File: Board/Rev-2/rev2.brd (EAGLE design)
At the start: 148.6 x 63.2 mm, 56 parts, among them IC1 74HC595N, T1 2N3904, T2 2N3904, T3 2N3904, T4 2N3904, T5 2N3904, T6 2N3904, T7 2N3904, T8 2N3904

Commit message: Board Generated
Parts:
- removed ESP-RESET, RESET: tackswitch, buttons:B3F-10XX
- removed PHOTOREG: 1kohm, resistor:0204/7
- removed R1: PHOTOCELLONB, LDR:ON_BOARD
- removed SL1: Flash, con-amp-quick:02PA
- added FLASH, GND_SWITCH, VCC_SWITCH: TOGGLE_SWITCH, Toggle Switch:TOGGLE_SWITCH
- added MCU-RESET, SETUP_MODE: tackswitch, buttons:B3F-10XX
- added PHOTO_REG: PHOTOCELLONB, LDR:ON_BOARD
- added PULLUP: 10kohm, resistor:0204/7
- added RESET_REG: 1kohm, resistor:0204/7
- added SV1: (no value), con-lstb:MA04-1
- moved RELR8 31.2 mm to (51.1, 24.0), turned to 90 degrees
- moved RELR6 29.3 mm to (94.8, 26.0), turned to 90 degrees
- moved D3 28.6 mm to (97.0, 15.1)
- moved RELR7 28.5 mm to (70.9, 27.0), turned to 90 degrees
- moved RELR5 28.3 mm to (117.7, 27.0), turned to 90 degrees
- moved D4 27.6 mm to (73.2, 16.1)
- moved D2 27.5 mm to (118.9, 15.1)
- moved D1 25.9 mm to (143.0, 14.1)
- moved PULLDOWN 24.9 mm to (20.0, 50.8)
- moved C1 24.9 mm to (13.6, 49.5)
- moved T5 24.7 mm to (119.3, 60.1)
- moved T6 24.7 mm to (96.4, 60.1)
- moved T8 24.7 mm to (50.7, 60.1)
- moved U$2 24.7 mm to (144.7, 29.2)
- moved CON-REL-1 24.7 mm to (135.8, 3.77)
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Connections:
- new net N$55: GND_SWITCH.ON, SV1.1
- new net N$56: SV1.4, VCC_SWITCH.ON
- net 3.5V: now also FLASH.OFF, PHOTO_REG.1, PULLUP.2, SETUP_MODE.2; no longer R1.1, RESET.2
- net ADC: now also PHOTO_REG.2, RESET_REG.2; no longer PHOTOREG.2, R1.2
- net GND: now also FLASH.ON, GND_SWITCH.IN, MCU-RESET.4, PULLUP.1, RESET_REG.1; no longer ESP-RESET.4, PHOTOREG.1, SL1.1
- net N$26: now also SETUP_MODE.4; no longer RESET.4
- net N$28: now also FLASH.IN; no longer SL1.2
- net N$29: now also SETUP_MODE.3; no longer RESET.3
- net N$31: now also MCU-RESET.2; no longer ESP-RESET.2
- net RX: now also SV1.2
- net TX: now also SV1.3
- net VCC: now also VCC_SWITCH.IN
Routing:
- net RX: track 52.8 -> 175.5 mm, vias 0 -> 7
- net TX: track 60.3 -> 167.4 mm, vias 0 -> 8
- net GND: track 399.1 -> 492.8 mm, vias 0 -> 1
- net N$47: track 30.0 -> 79.1 mm, vias 0 -> 3
- net N$27: track 34.1 -> 69.1 mm, vias 1 -> 0
- net N$55: track 0.00 -> 33.6 mm
- net N$28: track 44.2 -> 75.7 mm, vias 1 -> 0
- net N$48: track 32.0 -> 63.2 mm, vias 0 -> 1
- net RELAY7: track 78.2 -> 48.7 mm, vias 2 -> 1
- net VCC: track 206.3 -> 234.3 mm, vias 0 -> 1
- net N$49: track 33.5 -> 59.7 mm, vias 0 -> 1
- net RELAY1: track 121.2 -> 144.6 mm, vias 0 -> 3
- net N$56: track 0.00 -> 22.3 mm
- net 3.5V: track 266.5 -> 285.4 mm, vias 2 -> 6
- net SHCP: track 44.3 -> 61.8 mm, vias 3 -> 1
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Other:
- board size 148.6 x 63.2 mm -> 150.6 x 63.2 mm
- board text added: "Live"
- board text added: "Nutral"

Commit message: board updated
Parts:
- SV1: device con-lstb:MA04-1 -> con-lstb:MA06-2
- moved D1 7.28 mm to (141.0, 7.12)
- moved IC1 6.00 mm to (31.5, 6.31)
- moved U$1 5.00 mm to (14.6, 1.31), turned to 180 degrees
- moved PULLUP 4.00 mm to (22.0, 56.8), turned to 0 degrees
- moved T4 4.00 mm to (47.7, 5.85)
- moved REG1 2.83 mm to (22.0, 53.6)
- moved GND_SWITCH 2.24 mm to (141.0, 41.8)
- moved PULLDOWN 2.24 mm to (22.0, 49.8)
- moved U$2 2.24 mm to (143.7, 31.2)
- moved VCC_SWITCH 2.24 mm to (146.0, 41.8)
- moved SV1 1.54 mm to (146.0, 15.0), turned to 270 degrees
- moved D5 1.00 mm to (142.0, 55.3)
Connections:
- net 3.5V: now also SV1.4
- net CS0: now also SV1.6
- net GPIO10: now also SV1.7
- net GPIO5: now also SV1.5
- net GPIO9: now also SV1.9
- net MISO: now also SV1.8
- net MOSI: now also SV1.10
- net N$55: now also SV1.12; no longer SV1.1
- net N$56: now also SV1.2; no longer SV1.4
- net RX: now also SV1.3; no longer SV1.2
- net SCLK: now also SV1.11
- net TX: now also SV1.1; no longer SV1.3
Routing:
- net MISO: track 0.00 -> 211.1 mm, vias 0 -> 4
- net GPIO5: track 0.00 -> 175.1 mm, vias 0 -> 7
- net MOSI: track 0.00 -> 156.5 mm, vias 0 -> 7
- net GPIO9: track 0.00 -> 147.1 mm, vias 0 -> 7
- net GPIO10: track 0.00 -> 135.6 mm, vias 0 -> 6
- net CS0: track 0.00 -> 133.1 mm, vias 0 -> 11
- net SCLK: track 0.00 -> 123.4 mm, vias 0 -> 6
- net N$28: track 75.7 -> 42.5 mm, vias 0 -> 1
- net N$47: track 79.1 -> 48.8 mm, vias 3 -> 0
- net VCC: track 234.3 -> 262.4 mm
- net N$49: track 59.7 -> 34.3 mm
- net GND: track 492.8 -> 517.2 mm, vias 1 -> 2
- net RX: track 175.5 -> 199.2 mm, vias 7 -> 6
- net STCP: track 39.0 -> 59.0 mm, vias 1 -> 2
- net N$48: track 63.2 -> 43.9 mm, vias 1 -> 0
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
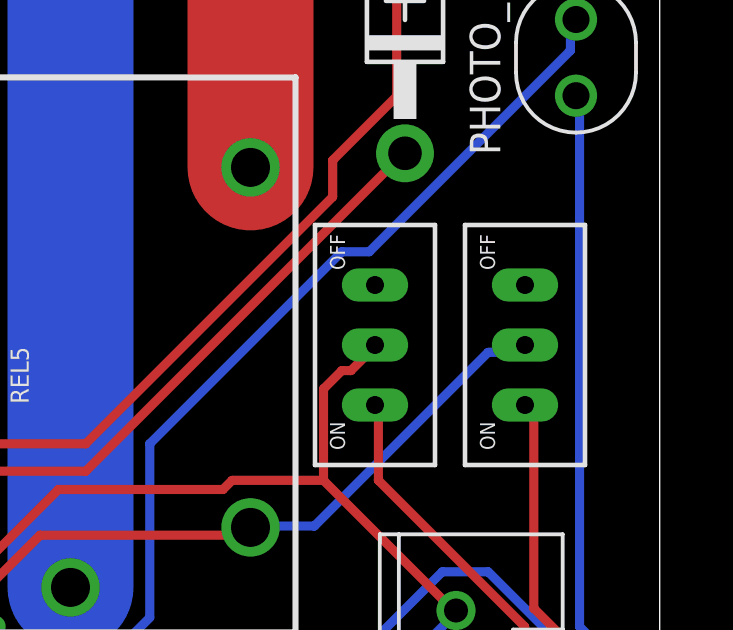
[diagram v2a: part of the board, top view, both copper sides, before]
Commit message: Reconnect option added
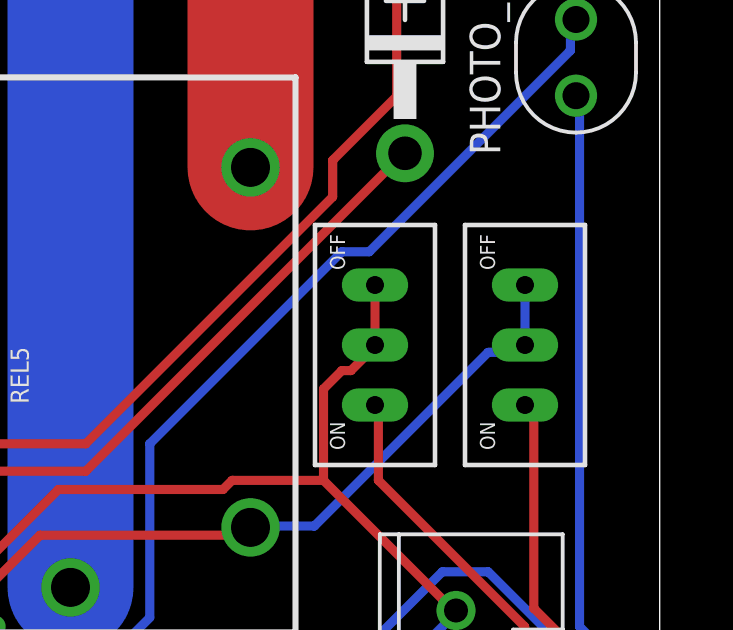
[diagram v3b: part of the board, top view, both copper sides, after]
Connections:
- net GND: now also GND_SWITCH.OFF
- net VCC: now also VCC_SWITCH.OFF
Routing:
- net VCC: track 262.4 -> 264.4 mm
- net GND: track 517.2 -> 519.2 mm
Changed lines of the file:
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@@
 <?xml version="1.0" encoding="utf-8"?>
 <!DOCTYPE eagle SYSTEM "eagle.dtd">
-<eagle version="9.6.2">
+<eagle version="9.3.0">
 <drawing>
 <settings>
@@
 </layers>
 <board>
-<fusionsync huburn="a.cGVyc29uYWw6dWUyYjdhYjY5" projecturn="a.cGVyc29uYWw6dWUyYjdhYjY5IzIwMTcwNzA4ODMxMDc1NTY" f3durn="urn:adsk.wipprod:dm.lineage:N7QxB5dOQdaGraEfLISNhQ" pcbguid="" lastpulledtime="" lastsyncedchangeguid="" latestrevisionid="b1b06610-b2d5-4e78-912c-e23e10fbecf6" lastsyncedrevisionid="b1b06610-b2d5-4e78-912c-e23e10fbecf6" lastboardhashguid="485106a5-8a0d-afa6-37d8-2fd97383113f" lastpushedtime="2020-07-16T18:36:36Z" linktopcb3d="true"/>
 <fusionteam huburn="a.cGVyc29uYWw6dWUyYjdhYjY5" projecturn="a.cGVyc29uYWw6dWUyYjdhYjY5IzIwMTcwNzA4ODMxMDc1NTY" folderUrn="urn:adsk.wipprod:fs.folder:co.GYMhV0F4TrqMDaTDnEaPZQ" urn="urn:adsk.wipprod:dm.lineage:VBlSYLAqTCGUwhFHxG7cdA"  versionUrn="urn:adsk.wipprod:fs.file:vf.VBlSYLAqTCGUwhFHxG7cdA?version=1" camFileUrn="" camFileVersionUrn="" lastpublishedchangeguid="a700656a-fba6-487a-2f14-d8389a4a237f"/>
 <plain>
@@
 <via x="87.4776" y="60.96" extent="1-16" drill="0.35"/>
 <via x="47.5488" y="38.4048" extent="1-16" drill="0.35"/>
+<contactref element="GND_SWITCH" pad="OFF"/>
+<wire x1="141.0097" y1="43.830659375" x2="141.0097" y2="45.830659375" width="0.3048" layer="1"/>
 </signal>
 <signal name="N$1">
@@
 <wire x1="54.864" y1="25.908" x2="54.7697" y2="25.670659375" width="0.3048" layer="16"/>
 <via x="128.6256" y="31.6992" extent="1-16" drill="0.35"/>
+<contactref element="VCC_SWITCH" pad="OFF"/>
+<wire x1="146.0097" y1="43.830659375" x2="146.0097" y2="45.830659375" width="0.3048" layer="16"/>
 </signal>
 <signal name="RX">
@@
 </note>
 <note version="8.3" severity="warning">
-Since Version 8.3, EAGLE supports Fusion synchronisation.
-This feature will not be available in this version and saving
-the document will break the link to the Fusion PCB feature.
-</note>
-<note version="8.3" severity="warning">
